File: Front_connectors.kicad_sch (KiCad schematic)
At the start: 6 parts

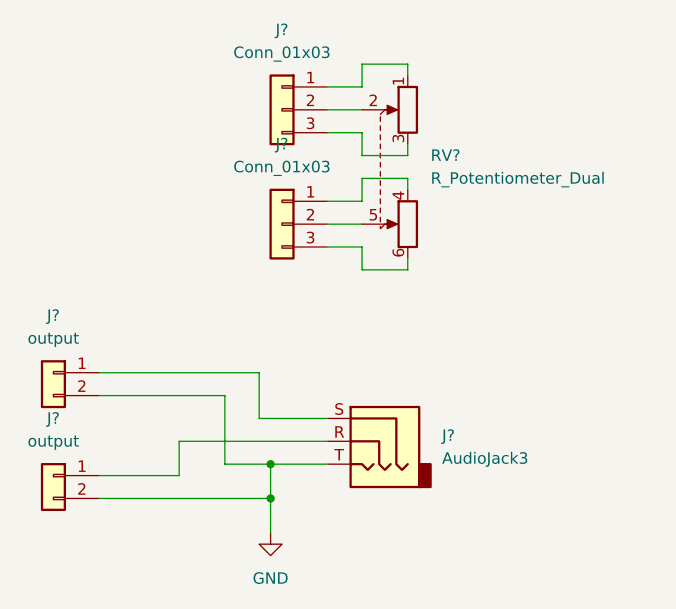
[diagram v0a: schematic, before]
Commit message: New power supply
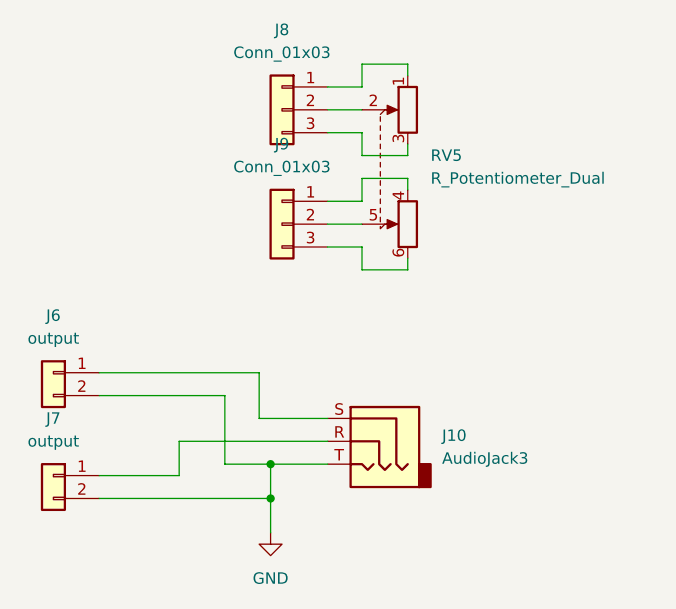
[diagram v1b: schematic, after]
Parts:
- gave numbers to parts that had none: 6
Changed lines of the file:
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@@
   (symbol (lib_id "Connector_Generic:Conn_01x03") (at 100.33 33.02 0) (mirror y) (unit 1)
     (in_bom yes) (on_board yes) (fields_autoplaced)
-    (property "Reference" "J?" (id 0) (at 100.33 24.13 0))
+    (property "Reference" "J8" (id 0) (at 100.33 24.13 0))
     (property "Value" "Conn_01x03" (id 1) (at 100.33 26.67 0))
     (property "Footprint" "spdf1626_lib:PinHeader_1x03_P2.54mm" (id 2) (at 100.33 33.02 0)
@@
   (symbol (lib_id "power:GND") (at 99.06 80.01 0) (unit 1)
     (in_bom yes) (on_board yes) (fields_autoplaced)
-    (property "Reference" "#PWR?" (id 0) (at 99.06 86.36 0)
+    (property "Reference" "#PWR026" (id 0) (at 99.06 86.36 0)
       (effects (font (size 1.27 1.27)) hide)
     )
@@
   (symbol (lib_id "Device:R_Potentiometer_Dual") (at 111.76 39.37 90) (mirror x) (unit 1)
     (in_bom yes) (on_board yes) (fields_autoplaced)
-    (property "Reference" "RV?" (id 0) (at 116.84 38.0999 90)
+    (property "Reference" "RV5" (id 0) (at 116.84 38.0999 90)
       (effects (font (size 1.27 1.27)) (justify right))
     )
@@
   (symbol (lib_id "Connector_Generic:Conn_01x02") (at 74.93 73.66 0) (mirror y) (unit 1)
     (in_bom yes) (on_board yes) (fields_autoplaced)
-    (property "Reference" "J?" (id 0) (at 74.93 67.31 0))
+    (property "Reference" "J7" (id 0) (at 74.93 67.31 0))
     (property "Value" "output" (id 1) (at 74.93 69.85 0))
     (property "Footprint" "spdf1626_lib:PinHeader_1x02_P2.54mm" (id 2) (at 74.93 73.66 0)
@@
   (symbol (lib_id "Connector_Generic:Conn_01x02") (at 74.93 62.23 0) (mirror y) (unit 1)
     (in_bom yes) (on_board yes) (fields_autoplaced)
-    (property "Reference" "J?" (id 0) (at 74.93 55.88 0))
+    (property "Reference" "J6" (id 0) (at 74.93 55.88 0))
     (property "Value" "output" (id 1) (at 74.93 58.42 0))
     (property "Footprint" "spdf1626_lib:PinHeader_1x02_P2.54mm" (id 2) (at 74.93 62.23 0)
@@
   (symbol (lib_id "Connector:AudioJack3") (at 110.49 69.85 0) (mirror y) (unit 1)
     (in_bom yes) (on_board yes) (fields_autoplaced)
-    (property "Reference" "J?" (id 0) (at 118.11 69.2149 0)
+    (property "Reference" "J10" (id 0) (at 118.11 69.2149 0)
       (effects (font (size 1.27 1.27)) (justify right))
     )
@@
   (symbol (lib_id "Connector_Generic:Conn_01x03") (at 100.33 45.72 0) (mirror y) (unit 1)
     (in_bom yes) (on_board yes) (fields_autoplaced)
-    (property "Reference" "J?" (id 0) (at 100.33 36.83 0))
+    (property "Reference" "J9" (id 0) (at 100.33 36.83 0))
     (property "Value" "Conn_01x03" (id 1) (at 100.33 39.37 0))
     (property "Footprint" "spdf1626_lib:PinHeader_1x03_P2.54mm" (id 2) (at 100.33 45.72 0)
